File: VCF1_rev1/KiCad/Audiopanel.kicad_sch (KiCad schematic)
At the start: 22 parts, among them J1 Thonk, SW1 SW_SPDT, SW2 SW_SPDT, SW3 SW_SPDT, SW4 SW_SPDT

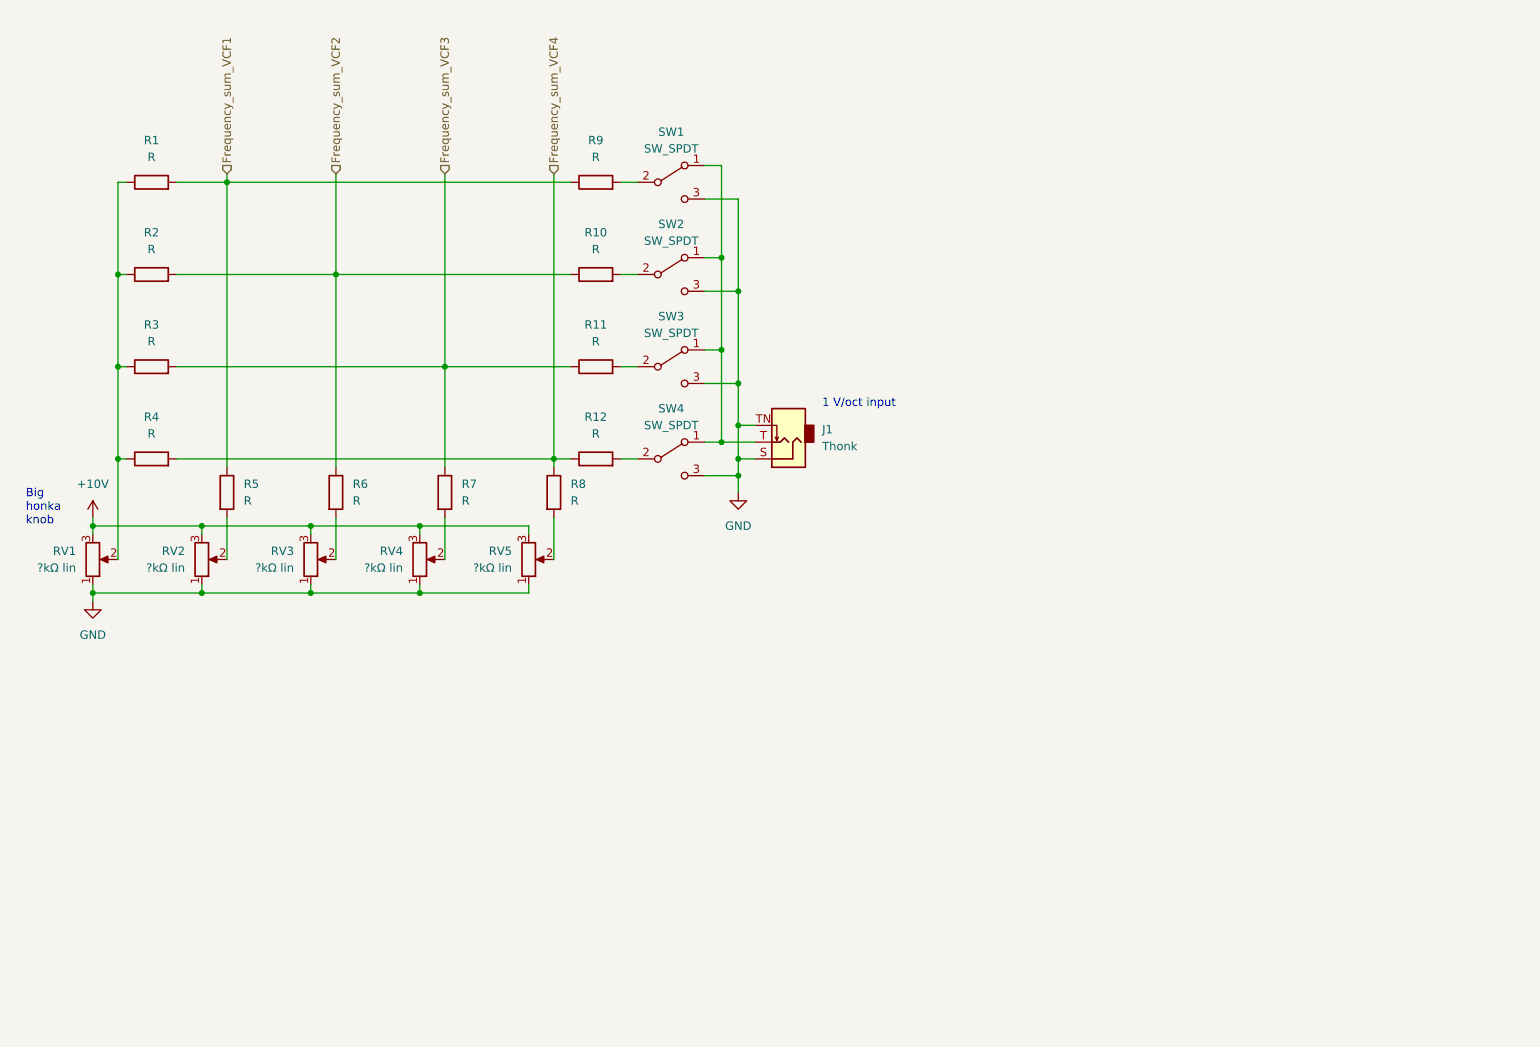
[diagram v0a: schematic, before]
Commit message: Cleaned up the first page with the overview and tried to make it a bit more readable.
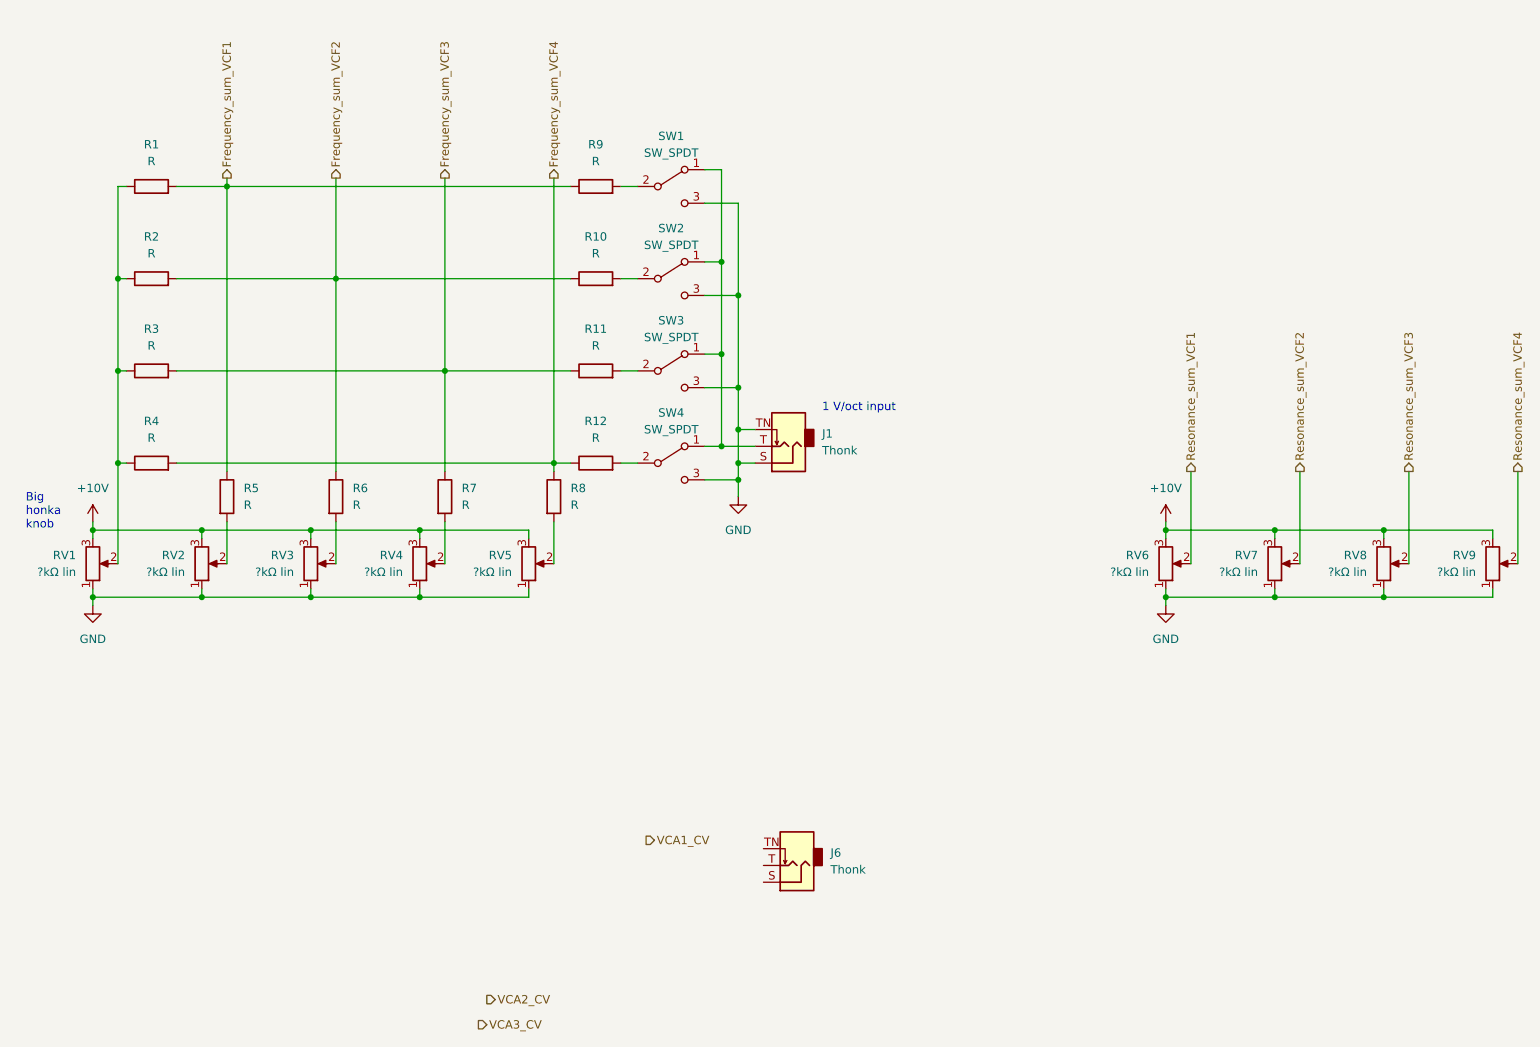
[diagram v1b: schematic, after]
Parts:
- added J6: Thonk, symbol Connector:AudioJack2_SwitchT
- added RV6, RV7, RV8, RV9: ?kΩ lin, symbol Device:R_Potentiometer
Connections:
- net +10V: now also RV6.3, RV7.3, RV8.3, RV9.3
- net GND: now also RV6.1, RV7.1, RV8.1, RV9.1
- new net Resonance_sum_VCF1: RV6.2
- new net Resonance_sum_VCF2: RV7.2
- new net Resonance_sum_VCF3: RV8.2
- new net Resonance_sum_VCF4: RV9.2
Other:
- moved on the sheet: J1, R1, R10, R11, R12, R2, R3, R4, R5, R6, R7, R8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

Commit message: Drew a better symbol for LM13700 because the other one was ugly.
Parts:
- R1, R10, R11, R12, R2, R3, R4, R5, R6, R7, R8, R9: footprint (none) -> Resistor_SMD:R_0603_1608Metric

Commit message: Cleanups, better names for the sheets etc.
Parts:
- removed J1, J6: Thonk, symbol Connector:AudioJack2_SwitchT
- removed R1, R10, R11, R12, R2, R3, R4, R5, R6, R7, R8, R9: R, Resistor_SMD:R_0603_1608Metric, symbol Device:R
- removed RV1, RV2, RV3, RV4, RV5, RV6, RV7, RV8, RV9: ?kΩ lin, symbol Device:R_Potentiometer
- removed SW1, SW2, SW3, SW4: SW_SPDT, symbol Switch:SW_SPDT
- added C1, C2, C4: 47pF, symbol Device:C
- added C3: 10pF, symbol Device:C
- added D1, D2, D3, D5, D6: D, symbol Device:D
- added D4: LED, symbol Device:LED
- added J2, J3, J4: AudioJack2_SwitchT, symbol Connector:AudioJack2_SwitchT
- added Q1: Q_NPN_BCE, symbol Device:Q_NPN_BCE
- added R23, R24, R25, R26, R27, R31, R32, R33: 100kΩ, Resistor_SMD:R_0603_1608Metric, symbol Device:R
- added R28: 330kΩ, Resistor_SMD:R_0603_1608Metric, symbol Device:R
- added R29: 4k7Ω, Resistor_SMD:R_0603_1608Metric, symbol Device:R
- added R30: TBD, Resistor_SMD:R_0603_1608Metric, symbol Device:R
- added RV10, RV11: 10kΩ lin, symbol Device:R_Potentiometer
- added U1: Opamp_Quad, symbol Device:Opamp_Quad
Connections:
- net GND: now also D3.2 (A), D6.1 (K), J2.S, J2.TN, J3.S, J4.S, J4.TN, R29.2, RV11.1, U1.10 (+), U1.12 (+), U1.3 (+), U1.5 (+)
- new net: C2.1, R24.1, R27.2, U1.6 (-)
- new net: C2.2, R27.1, RV10.3, U1.7
- new net: D1.2 (A), D2.1 (K)
- new net: D2.2 (A), D3.1 (K)
- new net: D4.1 (K), R30.1
- new net: Q1.2 (C), R30.2
- new net: C4.1, R31.2, R32.2, R33.2, U1.13 (-)
- new net: J3.T, R24.2
- new net: C1.2, R26.1, RV10.1, U1.1
- new net: C1.1, R23.1, R26.2, U1.2 (-)
- new net: D5.1 (K), D6.2 (A)
- new net: C3.1, R25.1, R28.2, U1.9 (-)
- new net: J4.T, R25.2
- new net: C3.2, R28.1, RV11.3, U1.8
- new net: J2.T, R23.2
- new net: D5.2 (A), Q1.3 (E)
- new net +12V: D4.2 (A)
- new net Audio_out: C4.2, R33.1, U1.14
- new net Input3: J3.TN
- new net Input_12: R31.1, RV10.2
- new net Input_3: D1.1 (K), Q1.1 (B), R29.1, R32.1, RV11.2
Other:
- note added: "Input 1"
- note added: "Input 2"
- note added: "Input 3"
- note added: "Overdrive indicator"
- note removed: "1 V/oct input"
- note removed: "Big honka knob"

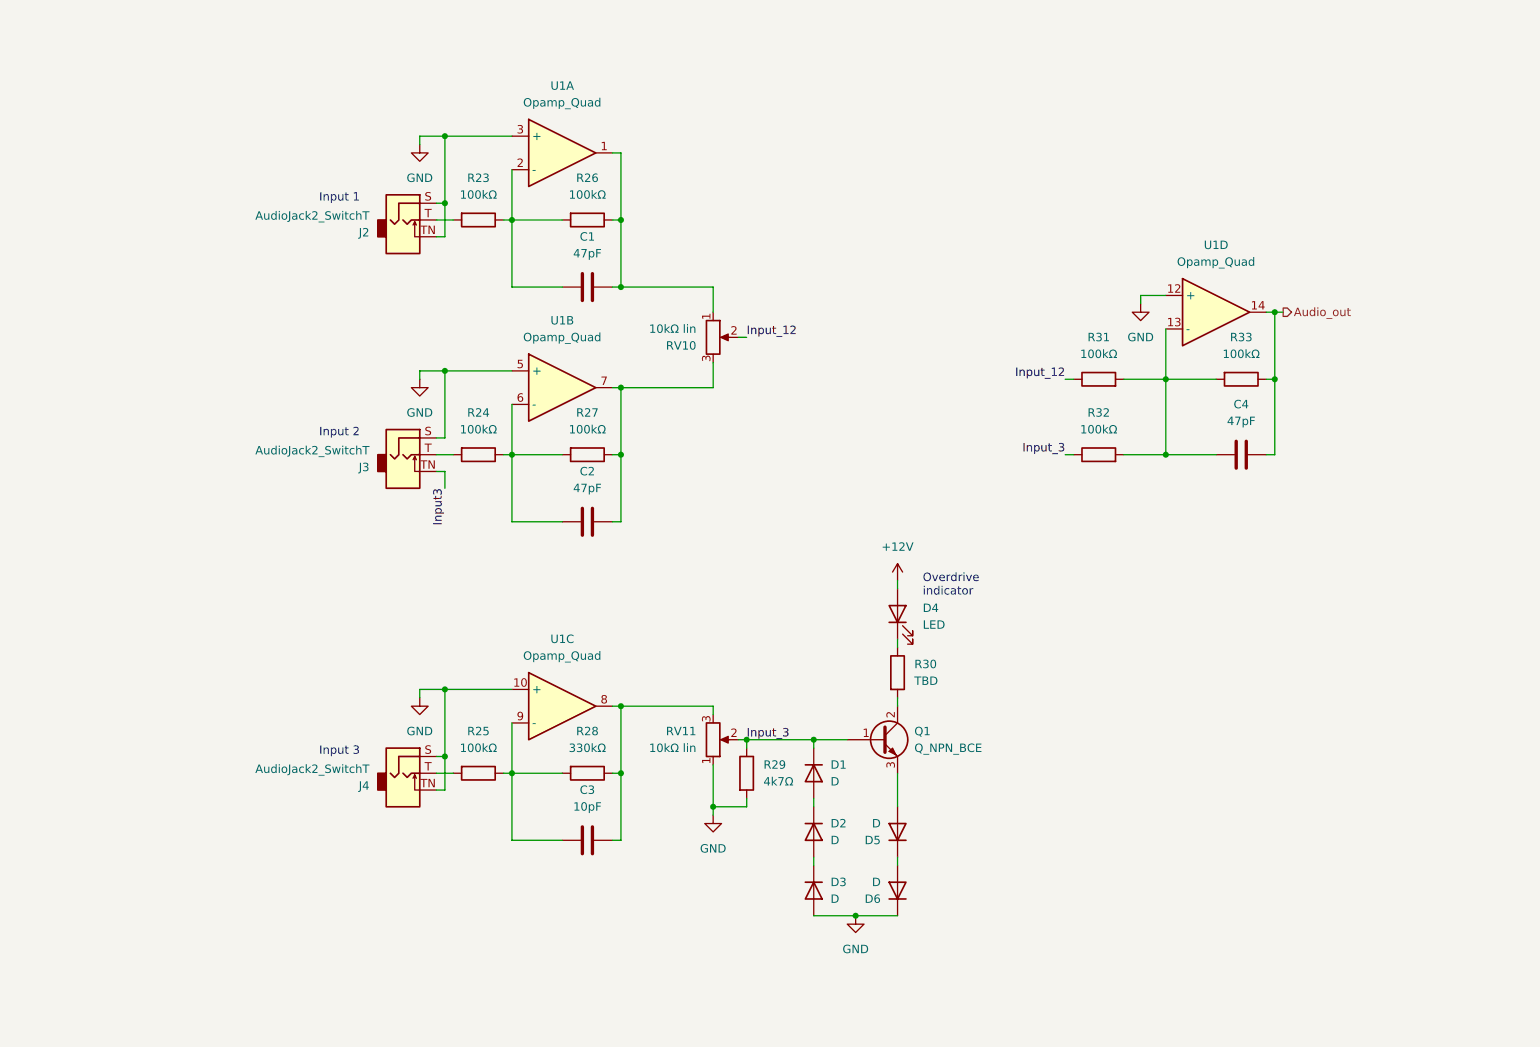
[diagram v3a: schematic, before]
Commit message: Started to populate the PCB and done some small fixes in the schematics.
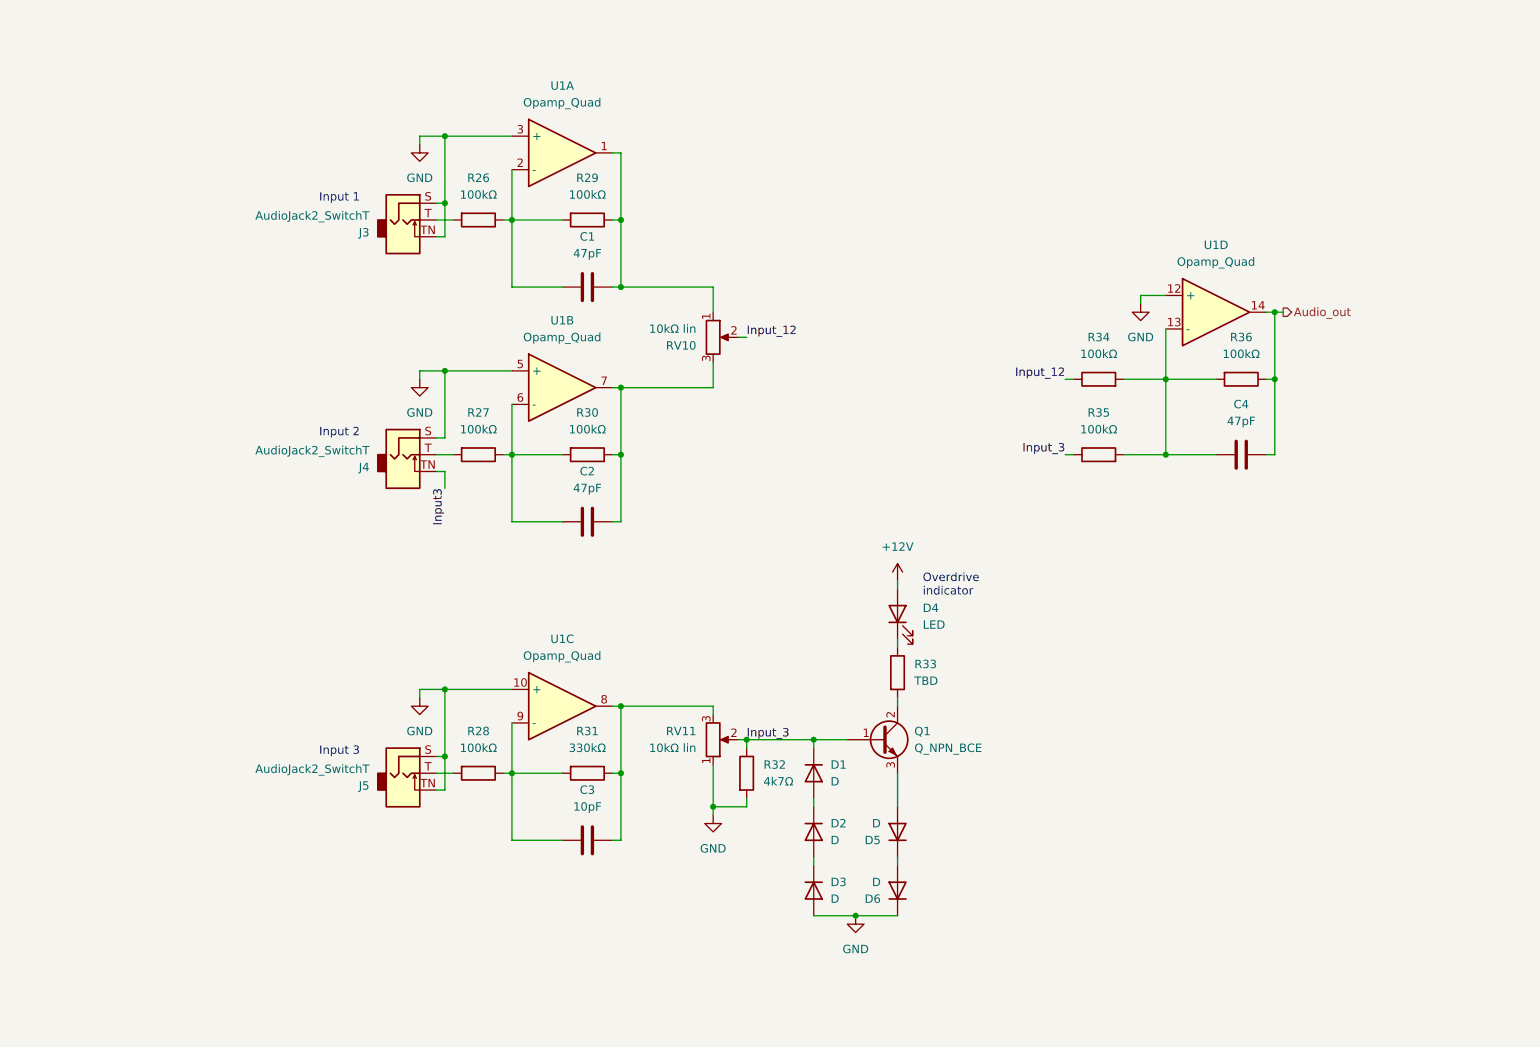
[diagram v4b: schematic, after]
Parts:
- C1, C2, C3, C4: footprint (none) -> Capacitor_SMD:C_0603_1608Metric
- D1, D2, D3, D5, D6: footprint (none) -> Diode_SMD:D_SOD-123
- D4: footprint (none) -> LED_THT:LED_D3.0mm
- U1: footprint (none) -> Package_SO:SOIC-14_3.9x8.7mm_P1.27mm
- renumbered J2 to J3, J3 to J4, J4 to J5, R23 to R26, R24 to R27, R25 to R28, R26 to R29, R27 to R30, R28 to R31, R29 to R32, R30 to R33, R31 to R34, R32 to R35, R33 to R36
